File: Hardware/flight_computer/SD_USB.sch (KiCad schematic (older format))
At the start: 2 parts, among them J2002 2908-05WB-MG, U2001 NUF2042XV6T1G

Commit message: added parts for DAN <3
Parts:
- J2002: symbol openDrone_parts:2908-05WB-MG -> flight_computer-rescue:2908-05WB-MG-openDrone_parts
- U2001: symbol openDrone_parts:NUF2042XV6T1G -> flight_computer-rescue:NUF2042XV6T1G-openDrone_parts
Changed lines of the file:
@@
 $EndDescr
 $Comp
-L openDrone_parts:NUF2042XV6T1G U2001
+L flight_computer-rescue:NUF2042XV6T1G-openDrone_parts U2001
 U 1 1 5F628055
 P 1950 2500
@@
 	2700 1700 2300 1700
 $Comp
-L openDrone_parts:2908-05WB-MG J2002
+L flight_computer-rescue:2908-05WB-MG-openDrone_parts J2002
 U 1 1 5F62DFF7
 P 2900 4350

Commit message: added more parts and datasheets
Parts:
- J2002: symbol flight_computer-rescue:2908-05WB-MG-openDrone_parts -> flight_computer-rescue:2908-05WB-MG-openDrone_parts-flight_computer-rescue
- U2001: symbol flight_computer-rescue:NUF2042XV6T1G-openDrone_parts -> flight_computer-rescue:NUF2042XV6T1G-openDrone_parts-flight_computer-rescue
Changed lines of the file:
@@
 $EndDescr
 $Comp
-L flight_computer-rescue:NUF2042XV6T1G-openDrone_parts U2001
+L flight_computer-rescue:NUF2042XV6T1G-openDrone_parts-flight_computer-rescue U2001
 U 1 1 5F628055
 P 1950 2500
@@
 	2700 1700 2300 1700
 $Comp
-L flight_computer-rescue:2908-05WB-MG-openDrone_parts J2002
+L flight_computer-rescue:2908-05WB-MG-openDrone_parts-flight_computer-rescue J2002
 U 1 1 5F62DFF7
 P 2900 4350

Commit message: Updates SD-USB and SERIAL schematics
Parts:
- removed J2002: 2908-05WB-MG, drone_footprints:2908-05WB-MG, symbol flight_computer-rescue:2908-05WB-MG-openDrone_parts-flight_computer-rescue
- removed U2001: NUF2042XV6T1G, drone_footprints:NUF2042XV6T1G, symbol flight_computer-rescue:NUF2042XV6T1G-openDrone_parts-flight_computer-rescue
- added J?: Micro_USB, Connectors_USB:USB_Micro-B_Molex_47346-0001, symbol openDrone_parts:Micro_USB
- added J?: MicroSD_molex, drone_footprints:2908-05WB-MG, symbol openDrone_parts:MicroSD_molex
- added R? (x5): R_100K, Resistors_SMD:R_0805, symbol openDrone_parts:R_100K
- added R? (x6): R_10K, Resistors_SMD:R_0805, symbol openDrone_parts:R_10K
- added U?: USB_Filter, drone_footprints:NUF2042XV6T1G, symbol openDrone_parts:USB_Filter
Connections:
- net labels added: OTG_N, OTG_P, PRESSURE_SENS, PRESSURE_SENS_IN, USB_GND_SHIELD, VDD_5V_IN, VDD_5V_SENS, VDD_SERVO, VDD_SERVO_SENS
- wire segments 15 -> 71

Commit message: Adds more sensor connections and communication with stm
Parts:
- removed R? (x6): R_10K, Resistors_SMD:R_0805, symbol openDrone_parts:R_10K
- removed U?: USB_Filter, drone_footprints:NUF2042XV6T1G, symbol openDrone_parts:USB_Filter
- added C?: C_0u1, Capacitors_SMD:C_0805, symbol openDrone_parts:C_0u1
- added R? (x2): R_22, Resistors_SMD:R_0805, symbol openDrone_parts:R_22
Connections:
- net labels added: OTG_FS_DM, OTG_FS_DP
- net labels removed: OTG_FS_N, OTG_FS_P, OTG_N, OTG_P, PRESSURE_SENS, PRESSURE_SENS_IN, USB_GND_SHIELD, VDD_5V_IN, VDD_5V_SENS, VDD_SERVO, VDD_SERVO_SENS
- wire segments 71 -> 40
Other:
- moved on the sheet: J?, R?

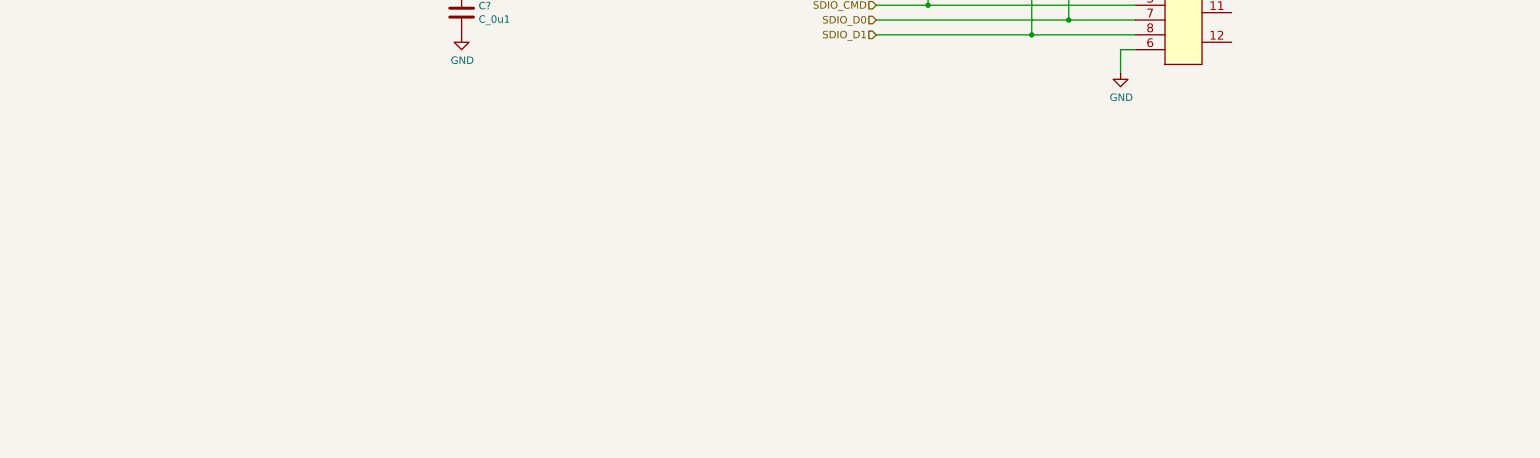
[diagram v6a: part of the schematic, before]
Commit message: Adds in regulators and filters
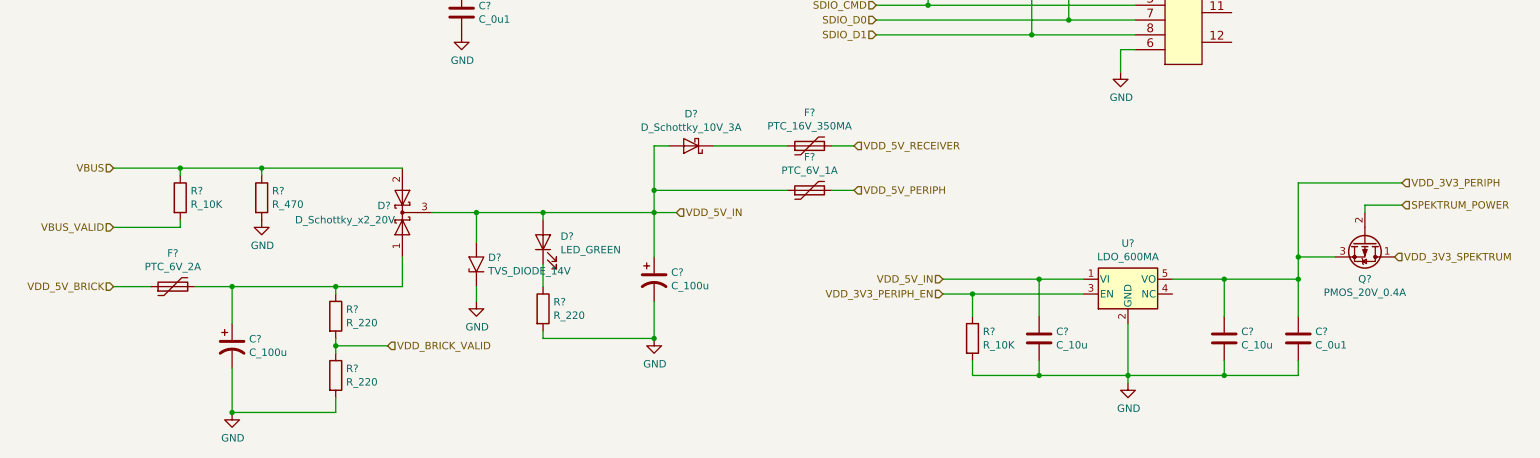
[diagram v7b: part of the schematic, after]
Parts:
- added C? (x2): C_100u, drone_footprints:10SGV100M6.3X6.1, symbol openDrone_parts:C_100u
- added C? (x2): C_10u, Capacitors_SMD:C_0805, symbol openDrone_parts:C_10u
- added C?: C_0u1, Capacitors_SMD:C_0805, symbol openDrone_parts:C_0u1
- added D?: D_Schottky_x2_20V, drone_footprints:SOT1061, symbol openDrone_parts:D_Schottky_x2_20V
- added D?: LED_GREEN, LEDs:LED_0603_HandSoldering, symbol openDrone_parts:LED_GREEN
- added D?: D_Schottky_10V_3A, Diodes_SMD:D_SOD-323F, symbol openDrone_parts:D_Schottky_10V_3A
- added D?: TVS_DIODE_14V, Capacitors_SMD:C_0402, symbol openDrone_parts:TVS_DIODE_14V
- added F?: PTC_6V_2A, Fuse_Holders_and_Fuses:Fuse_SMD1206_HandSoldering, symbol openDrone_parts:PTC_6V_2A
- added F?: PTC_16V_350MA, Resistors_SMD:R_0805_HandSoldering, symbol openDrone_parts:PTC_16V_350MA
- added F?: PTC_6V_1A, Resistors_SMD:R_0805_HandSoldering, symbol openDrone_parts:PTC_6V_1A
- added Q?: PMOS_20V_0.4A, TO_SOT_Packages_SMD:SOT-323_SC-70, symbol openDrone_parts:PMOS_20V_0.4A
- added R? (x2): R_10K, Resistors_SMD:R_0805, symbol openDrone_parts:R_10K
- added R? (x3): R_220, Resistors_SMD:R_0805, symbol openDrone_parts:R_220
- added R?: R_470, Resistors_SMD:R_0805, symbol openDrone_parts:R_470
- added U?: LDO_600MA, drone_footprints:SOT-25_DIO, symbol openDrone_parts:LDO_600MA
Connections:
- net GND: now also C?.2, C?.2, C?.2, C?.2, C?.2, D?.1 (A1), R?.2, R?.2, R?.2, R?.2, U?.2 (GND)
- net VBUS: now also D?.2 (A), R?.1, R?.1
- new net: C?.1, D?.1 (A), F?.2, R?.1
- new net: D?.1 (K), R?.1
- new net: D?.1 (K), F?.1
- new net SPEKTRUM_POWER: Q?.2 (G)
- new net VBUS_VALID: R?.2
- new net VDD_3V3_PERIPH: C?.1, C?.1, Q?.3 (S), U?.5 (VO)
- new net VDD_3V3_PERIPH_EN: R?.1, U?.3 (EN)
- new net VDD_3V3_SPEKTRUM: Q?.1 (D)
- new net VDD_5V_BRICK: F?.1
- new net VDD_5V_IN: C?.1, C?.1, D?.2 (A), D?.2 (A), D?.2 (A2), D?.3 (K), F?.1, U?.1 (VI)
- new net VDD_5V_PERIPH: F?.2
- new net VDD_5V_RECEIVER: F?.2
- new net VDD_BRICK_VALID: R?.1, R?.2

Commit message: added components, rerranged things to slow down dan
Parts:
- removed C? (x2): C_100u, drone_footprints:10SGV100M6.3X6.1, symbol openDrone_parts:C_100u
- removed C? (x2): C_10u, Capacitors_SMD:C_0805, symbol openDrone_parts:C_10u
- removed C?: C_0u1, Capacitors_SMD:C_0805, symbol openDrone_parts:C_0u1
- removed D?: D_Schottky_x2_20V, drone_footprints:SOT1061, symbol openDrone_parts:D_Schottky_x2_20V
- removed D?: LED_GREEN, LEDs:LED_0603_HandSoldering, symbol openDrone_parts:LED_GREEN
- removed D?: D_Schottky_10V_3A, Diodes_SMD:D_SOD-323F, symbol openDrone_parts:D_Schottky_10V_3A
- removed D?: TVS_DIODE_14V, Capacitors_SMD:C_0402, symbol openDrone_parts:TVS_DIODE_14V
- removed F?: PTC_6V_2A, Fuse_Holders_and_Fuses:Fuse_SMD1206_HandSoldering, symbol openDrone_parts:PTC_6V_2A
- removed F?: PTC_16V_350MA, Resistors_SMD:R_0805_HandSoldering, symbol openDrone_parts:PTC_16V_350MA
- removed F?: PTC_6V_1A, Resistors_SMD:R_0805_HandSoldering, symbol openDrone_parts:PTC_6V_1A
- removed Q?: PMOS_20V_0.4A, TO_SOT_Packages_SMD:SOT-323_SC-70, symbol openDrone_parts:PMOS_20V_0.4A
- removed R? (x2): R_10K, Resistors_SMD:R_0805, symbol openDrone_parts:R_10K
- removed R? (x3): R_220, Resistors_SMD:R_0805, symbol openDrone_parts:R_220
- removed R?: R_470, Resistors_SMD:R_0805, symbol openDrone_parts:R_470
- removed U?: LDO_600MA, drone_footprints:SOT-25_DIO, symbol openDrone_parts:LDO_600MA
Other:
- note added: "BATTERY = VBAT\nBUCK CONVERTER OUTPUT (VDD_5V_BRICK) = VDD_5V_BUCK\nUSB POWER (VBUS) = VDD_5V_USB\nRADIO 5V (VDD_5V_RECEIVER) = VDD_5V_RADIO\nGENERAL 5V (VDD_5V_IN) = VDD_5V_IN\nTELEM/FRSKY (VDD_5V_PERIPH) = VDD_5V_TELEM\nSTM POWER (FMU_VDD_3V3) = VDD_3V3_STM\nSENSORS POWER (VDD_3V3_SENSORS) = VDD_3V3_SENSORS\nRADIO POWER (VDD_3V3_SPEKTRUM) = RADIO_VDD_3V3\n"
